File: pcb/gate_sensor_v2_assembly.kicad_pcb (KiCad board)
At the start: 2 copper layers, 75 x 66 mm, 14 parts, among them J2 PWR_IN_ScrewTerm, J4 PWR_SW_JST_PH_2pin, U1 Arduino_Nano_Socket, U2 RXB6_433MHz_DirectSolder, U3 Heltec_LoRa32_V3

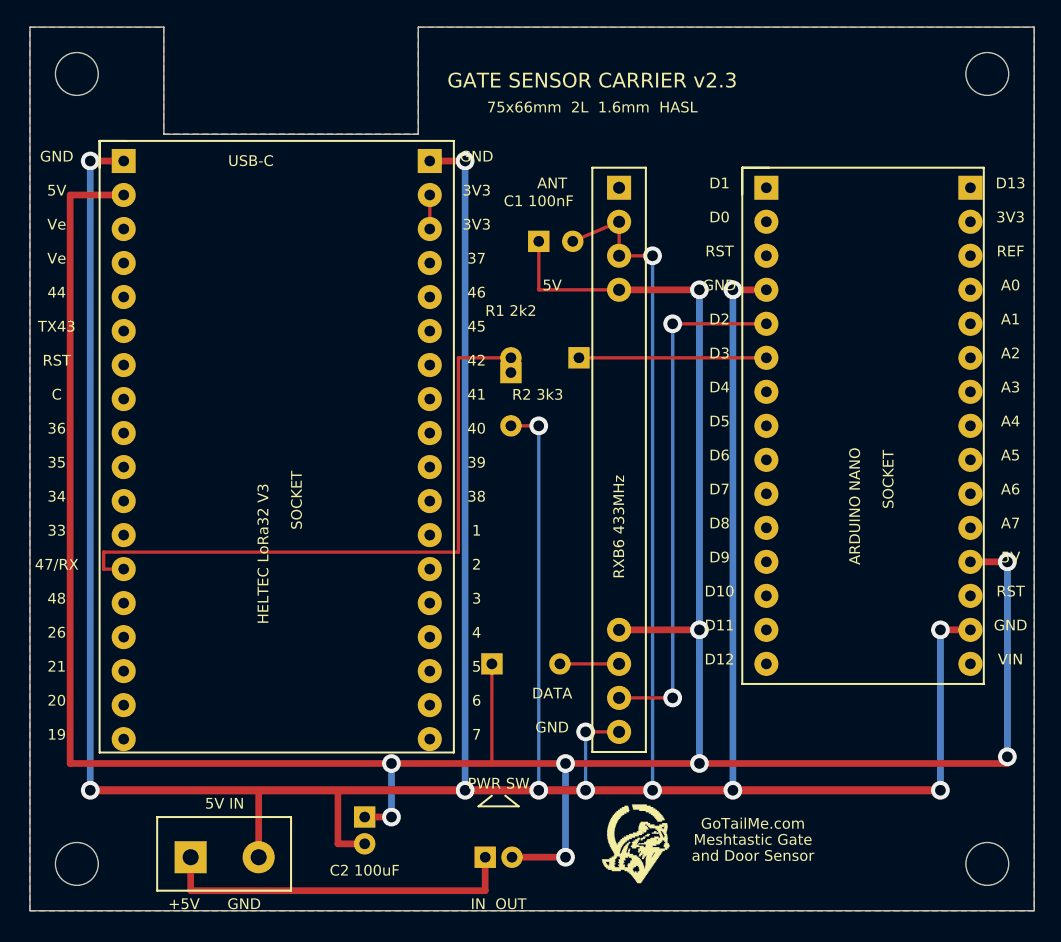
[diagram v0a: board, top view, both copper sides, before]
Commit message: Fix Arduino Nano left/right pin swap and digital pin order
The Nano socket had analog/power pins on the RIGHT and digital pins
on the LEFT — reversed from the real board. Digital pin order was also
inverted (D1 at USB end instead of D12). Verified against 4 reference
pinout images.

- Swap NL/NR arrays: LEFT=analog/power, RIGHT=digital (descending)
- Re-route D3 (R10→R1) all-F.Cu via top of board
- Re-route D2 (R11→RXB6 DATA) all-F.Cu via right board edge
- Simplify V5 routing: tap existing RXB6 B.Cu column at X=50
- Update GND drops for new pin positions (L14, R12)
- Trim V5 bus to end at last connection (X=50)
- DRC: 0 violations, 0 unconnected pads
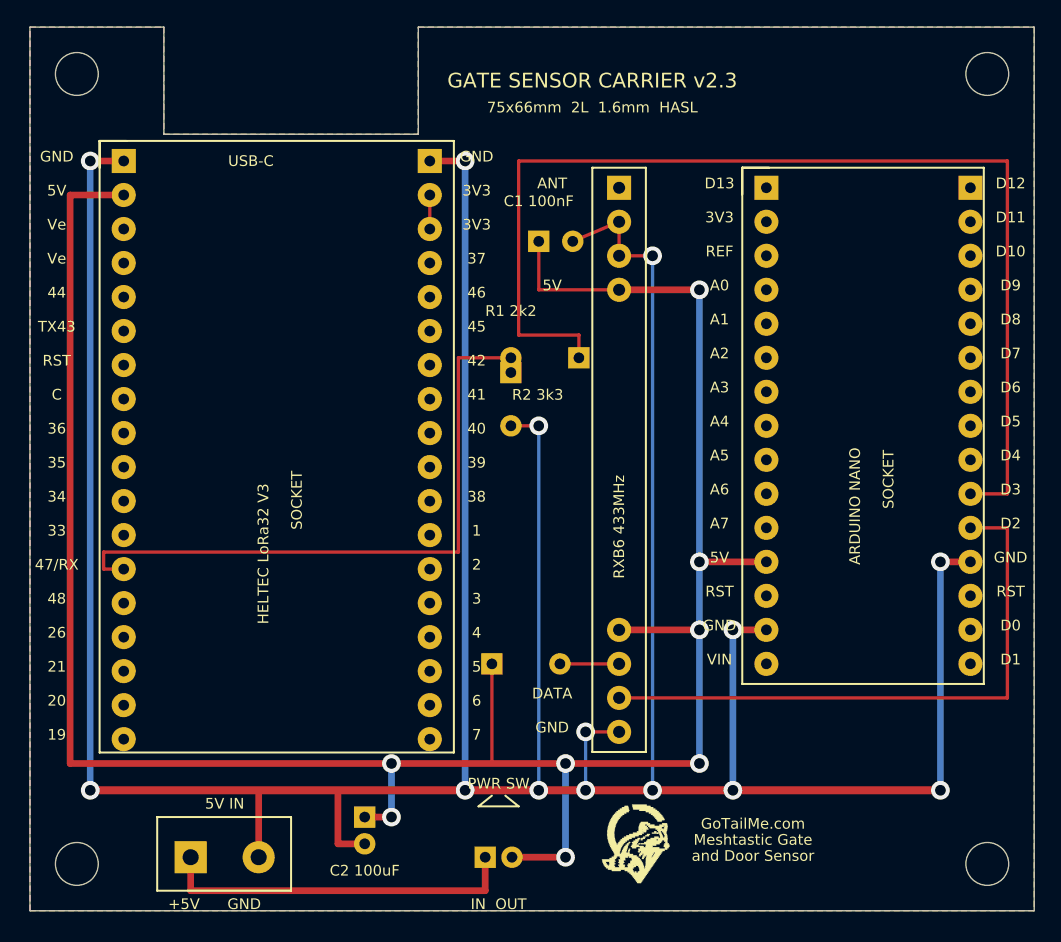
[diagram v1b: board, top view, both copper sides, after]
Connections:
- U1 pad L12: (no net) -> 5V
- U1 pad L14: (no net) -> GND
- U1 pad L4: GND -> (no net)
- U1 pad L5: D2 -> (no net)
- U1 pad L6: D3 -> (no net)
- U1 pad R10: (no net) -> D3
- U1 pad R11: (no net) -> D2
- U1 pad R12: 5V -> GND
- U1 pad R14: GND -> (no net)
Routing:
- net D3: track 14.0 -> 83.3 mm
- net 5V: track 215.7 -> 179.9 mm, vias 9 -> 8
- net GND: track 312.6 -> 292.3 mm
- net D2: track 38.9 -> 44.5 mm, vias 2 -> 0
